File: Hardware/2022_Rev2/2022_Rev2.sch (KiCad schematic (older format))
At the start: 14 parts

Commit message: Added Heirarchical Labels inside the 12V sheet
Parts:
- Conn? (x2): symbol MRDT_Connectors:AndersonPP -> 2022_Rev2-rescue:AndersonPP-MRDT_Connectors
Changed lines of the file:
@@
 $EndSheet
 $Sheet
-S 8200 1050 2350 2500
+S 1300 1000 2350 2500
 U 62118F7B
 F0 "TEENSY" 50
@@
 $EndSheet
 $Comp
-L MRDT_Connectors:AndersonPP Conn?
+L 2022_Rev2-rescue:AndersonPP-MRDT_Connectors Conn?
 U 4 1 62120188
 P 10350 5800
@@
 $EndComp
 $Comp
-L MRDT_Connectors:AndersonPP Conn?
+L 2022_Rev2-rescue:AndersonPP-MRDT_Connectors Conn?
 U 1 1 6212018E
 P 10350 6300
@@
 Text GLabel 2850 4950 1    50   Output ~ 0
 5V
-Text GLabel 1100 1300 0    50   Input ~ 0
+Text GLabel 8400 1000 0    50   Input ~ 0
 PV
 Wire Wire Line
-	1100 1300 1200 1300
+	8400 1000 8500 1000
 Text GLabel 4650 1200 0    50   Input ~ 0
 5V
@@
 	4650 1200 4750 1200
 $Sheet
-S 1200 1200 2100 2250
+S 8500 900  2100 2250
 U 6217B740
 F0 "BucksAndersons" 50
 F1 "BuckAndersons.sch" 50
-F2 "PV" I L 1200 1300 50
+F2 "PV" I L 8500 1000 50
 $EndSheet
 $EndSCHEMATC

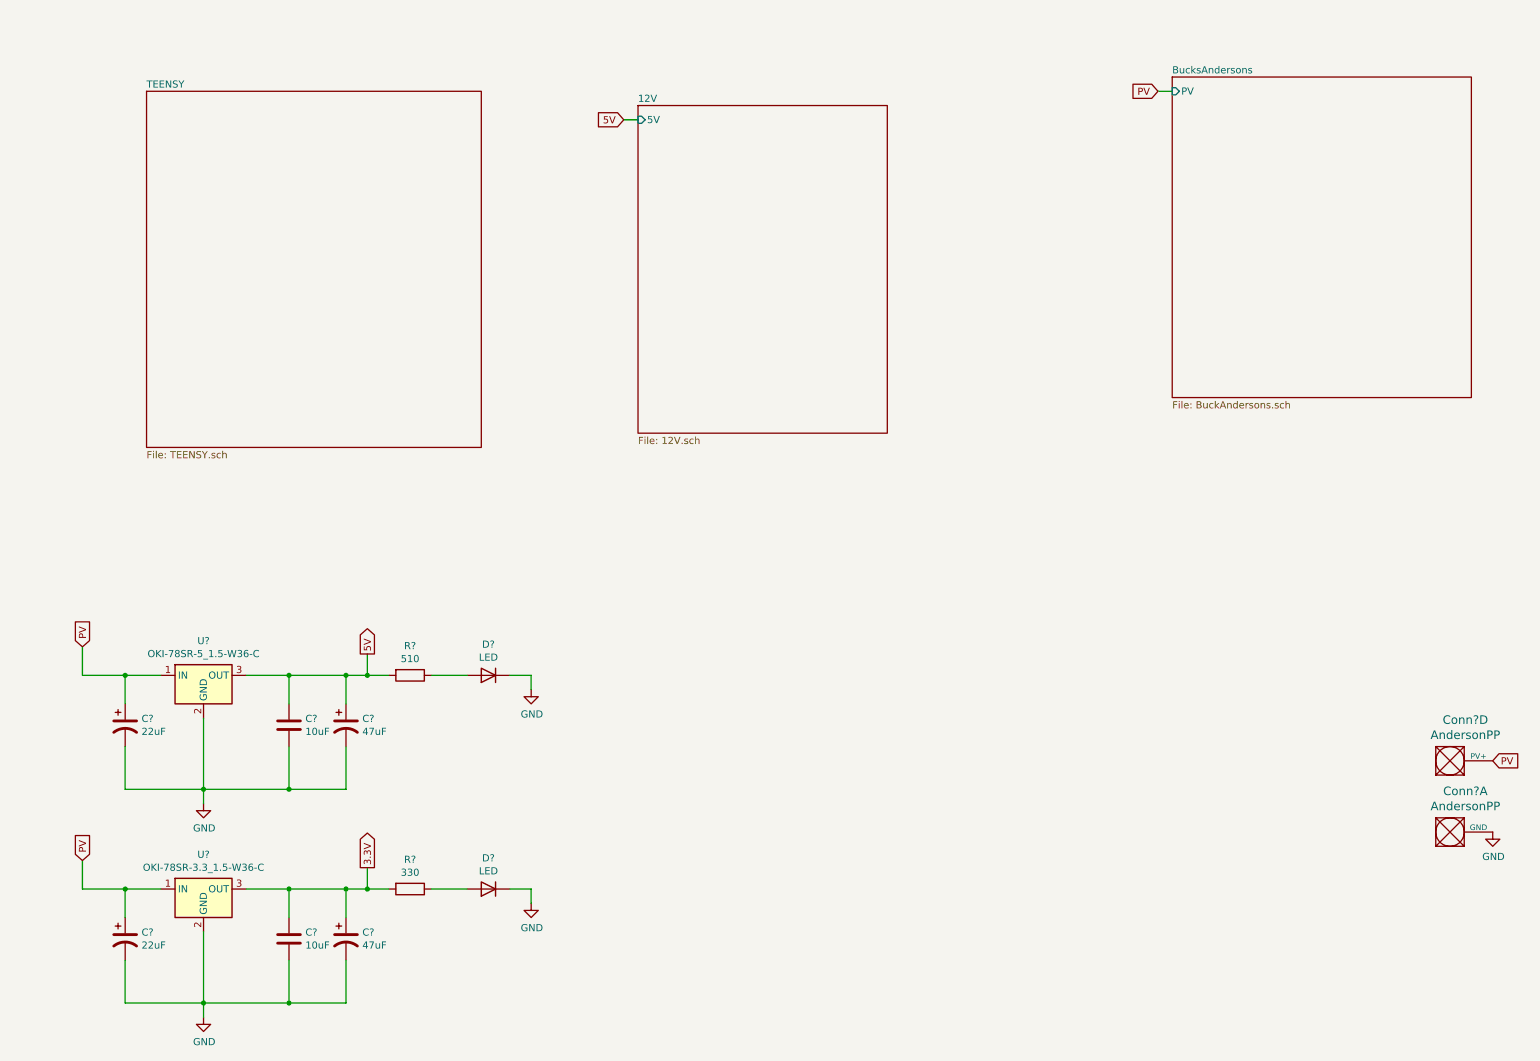
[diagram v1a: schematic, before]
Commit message: Organized some stuff and added Teensy connections
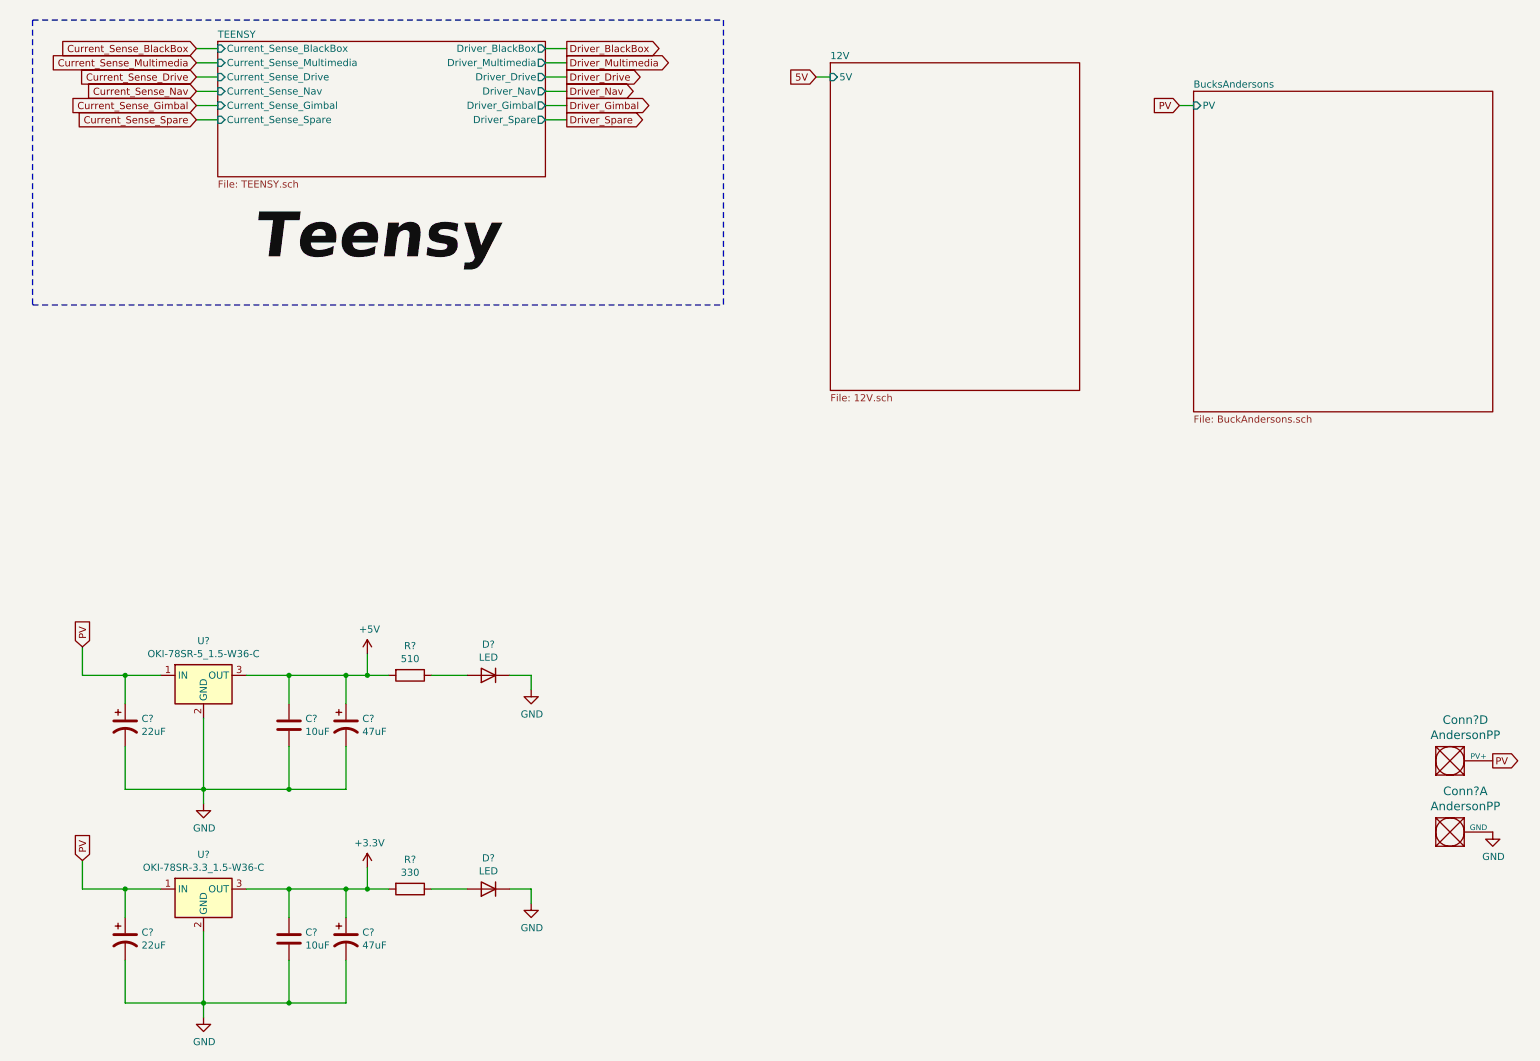
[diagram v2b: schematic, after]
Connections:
- net 5V: no longer C?.1, C?.1, R?.2, U?.3 (OUT)
- net 3.3V renamed +3V3
- new net +5V: C?.1, C?.1, R?.2, U?.3 (OUT)
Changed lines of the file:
@@
 EESchema Schematic File Version 4
+LIBS:2022_Rev2-cache
 EELAYER 30 0
 EELAYER END
@@
 $EndDescr
 $Sheet
-S 4750 1100 1750 2300
+S 6100 800  1750 2300
 U 62118E70
 F0 "12V" 50
 F1 "12V.sch" 50
-F2 "5V" I L 4750 1200 50
+F2 "5V" I L 6100 900 50
 $EndSheet
 $Sheet
-S 1300 1000 2350 2500
+S 1800 650  2300 950
 U 62118F7B
 F0 "TEENSY" 50
 F1 "TEENSY.sch" 50
+F2 "Current_Sense_BlackBox" I L 1800 700 50
+F3 "Current_Sense_Multimedia" I L 1800 800 50
+F4 "Current_Sense_Drive" I L 1800 900 50
+F5 "Current_Sense_Nav" I L 1800 1000 50
+F6 "Current_Sense_Gimbal" I L 1800 1100 50
+F7 "Current_Sense_Spare" I L 1800 1200 50
+F8 "Driver_BlackBox" O R 4100 700 50
+F9 "Driver_Multimedia" O R 4100 800 50
+F10 "Driver_Drive" O R 4100 900 50
+F11 "Driver_Nav" O R 4100 1000 50
+F12 "Driver_Gimbal" O R 4100 1100 50
+F13 "Driver_Spare" O R 4100 1200 50
 $EndSheet
 $Comp
@@
 	1    0    0    -1
 $EndComp
-Text GLabel 10750 5700 2    50   Input ~ 0
+Text GLabel 10750 5700 2    50   Output ~ 0
 PV
 Text GLabel 850  4900 1    50   Input ~ 0
@@
 	1    0    0    -1
 $EndComp
-Text GLabel 2850 6450 1    50   Output ~ 0
-3.3V
-Text GLabel 2850 4950 1    50   Output ~ 0
+Text GLabel 8550 1100 0    50   Input ~ 0
+PV
+Wire Wire Line
+	8550 1100 8650 1100
+Text GLabel 6000 900  0    50   Input ~ 0
 5V
-Text GLabel 8400 1000 0    50   Input ~ 0
-PV
-Wire Wire Line
-	8400 1000 8500 1000
-Text GLabel 4650 1200 0    50   Input ~ 0
-5V
-Wire Wire Line
-	4650 1200 4750 1200
+Wire Wire Line
+	6000 900  6100 900
 $Sheet
-S 8500 900  2100 2250
+S 8650 1000 2100 2250
 U 6217B740
 F0 "BucksAndersons" 50
 F1 "BuckAndersons.sch" 50
-F2 "PV" I L 8500 1000 50
+F2 "PV" I L 8650 1100 50
 $EndSheet
+$Comp
+L power:+3.3V #PWR?
+U 1 1 62206317
+P 2850 6450
+F 0 "#PWR?" H 2850 6300 50  0001 C CNN
+F 1 "+3.3V" H 2865 6623 50  0000 C CNN
+F 2 "" H 2850 6450 50  0001 C CNN
+F 3 "" H 2850 6450 50  0001 C CNN
+	1    2850 6450
+	1    0    0    -1
+$EndComp
+$Comp
+L power:+5V #PWR?
+U 1 1 62206CB8
+P 2850 4950
+F 0 "#PWR?" H 2850 4800 50  0001 C CNN
+F 1 "+5V" H 2865 5123 50  0000 C CNN
+F 2 "" H 2850 4950 50  0001 C CNN
+F 3 "" H 2850 4950 50  0001 C CNN
+	1    2850 4950
+	1    0    0    -1
+$EndComp
+Text GLabel 1650 700  0    50   Input ~ 0
+Current_Sense_BlackBox
+Text GLabel 1650 800  0    50   Input ~ 0
+Current_Sense_Multimedia
+Text GLabel 1650 900  0    50   Input ~ 0
+Current_Sense_Drive
+Text GLabel 1650 1100 0    50   Input ~ 0
+Current_Sense_Gimbal
+Text GLabel 1650 1200 0    50   Input ~ 0
+Current_Sense_Spare
+Text GLabel 1650 1000 0    50   Input ~ 0
+Current_Sense_Nav
+Wire Wire Line
+	1650 700  1800 700
+Wire Wire Line
+	1800 800  1650 800
+Wire Wire Line
+	1650 900  1800 900
+Wire Wire Line
+	1800 1000 1650 1000
+Wire Wire Line
+	1650 1100 1800 1100
+Wire Wire Line
+	1800 1200 1650 1200
+Text GLabel 4250 700  2    50   Output ~ 0
+Driver_BlackBox
+Wire Wire Line
+	4100 700  4250 700
+Text GLabel 4250 800  2    50   Output ~ 0
+Driver_Multimedia
+Wire Wire Line
+	4100 800  4250 800
+Text GLabel 4250 900  2    50   Output ~ 0
+Driver_Drive
+Wire Wire Line
+	4100 900  4250 900
+Text GLabel 4250 1000 2    50   Output ~ 0
+Driver_Nav
+Wire Wire Line
+	4100 1000 4250 1000
+Text GLabel 4250 1100 2    50   Output ~ 0
+Driver_Gimbal
+Wire Wire Line
+	4100 1100 4250 1100
+Text GLabel 4250 1200 2    50   Output ~ 0
+Driver_Spare
+Wire Wire Line
+	4100 1200 4250 1200
+Wire Notes Line
+	500  500  5350 500
+Text Label 2050 2250 0    315  Italic 63
+Teensy
+Wire Notes Line
+	500  2500 5350 2500
+Wire Notes Line
+	5350 500  5350 2500
+Wire Notes Line
+	500  500  500  2500
 $EndSCHEMATC

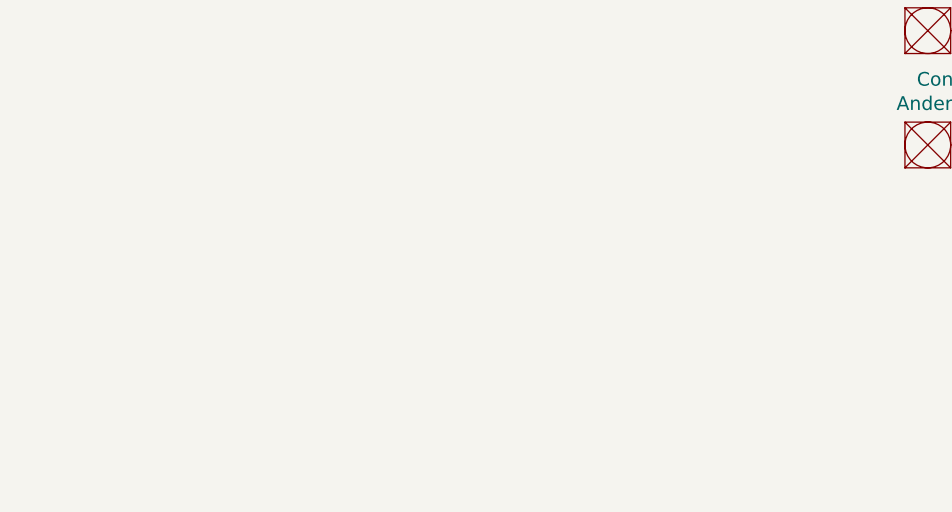
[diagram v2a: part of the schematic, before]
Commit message: Named the 12Volt Board
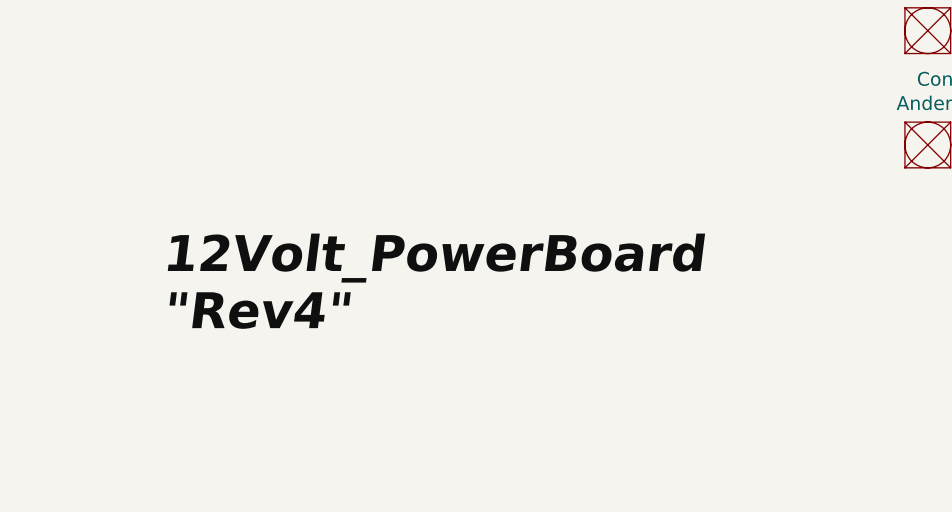
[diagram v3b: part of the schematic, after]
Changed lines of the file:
@@
 Wire Notes Line
 	500  500  500  2500
+Text Label 7100 6800 0    157  Italic 31
+12Volt_PowerBoard
+Text Label 7100 7050 0    157  Italic 31
+"Rev4"
 $EndSCHEMATC

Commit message: Tiva implementation
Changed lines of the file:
@@
 EESchema Schematic File Version 4
-LIBS:2022_Rev2-cache
 EELAYER 30 0
 EELAYER END
@@
 Wire Notes Line
 	500  500  5350 500
-Text Label 2050 2250 0    315  Italic 63
-Teensy
+Text Label 450  2500 0    315  Italic 63
+Tiva
 Wire Notes Line
 	500  2500 5350 2500

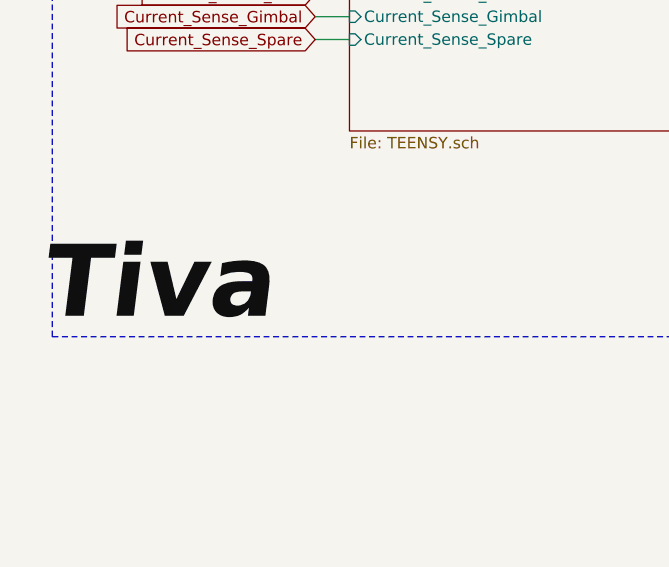
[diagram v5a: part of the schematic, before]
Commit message: 12v switch circuits added
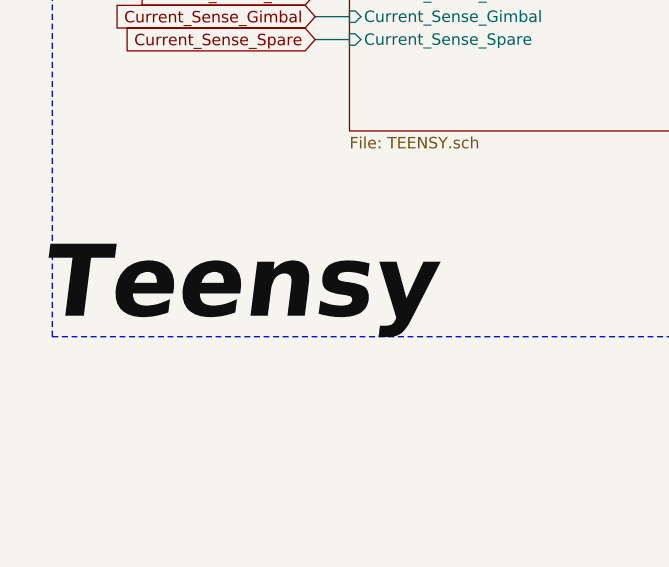
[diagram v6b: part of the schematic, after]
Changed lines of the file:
@@
 	500  500  5350 500
 Text Label 450  2500 0    315  Italic 63
-Tiva
+Teensy
 Wire Notes Line
 	500  2500 5350 2500
